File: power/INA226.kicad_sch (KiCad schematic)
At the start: 5 parts, among them U4 INA226

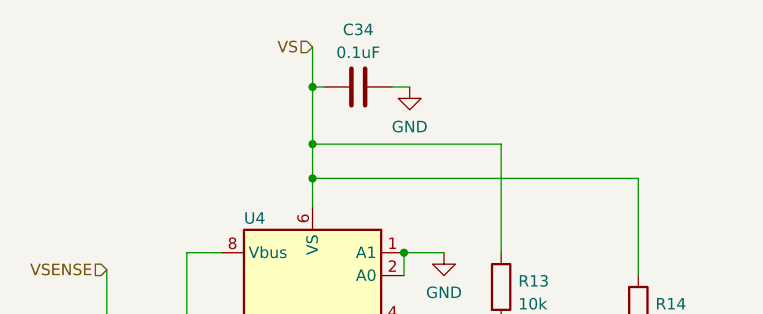
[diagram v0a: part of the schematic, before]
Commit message: Feat: Completed footprint assignment, began part placement
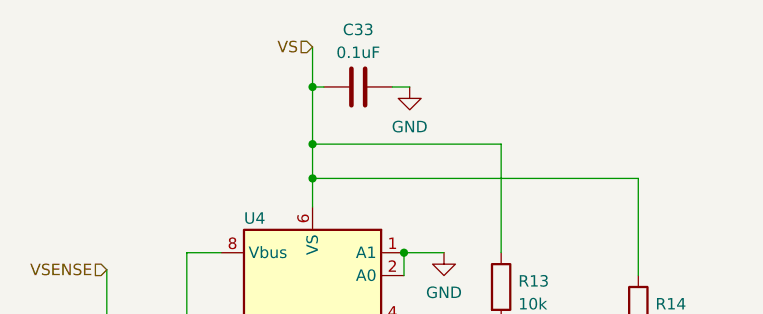
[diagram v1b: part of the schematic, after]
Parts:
- C33: renamed from C34; footprint (none) -> Capacitor_SMD:C_0603_1608Metric
- R13, R14: footprint (none) -> Resistor_SMD:R_0603_1608Metric
- R18: footprint (none) -> Resistor_SMD:R_2512_6332Metric
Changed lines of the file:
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@@
   (symbol (lib_id "Device:C") (at 153.67 64.77 90) (unit 1)
     (in_bom yes) (on_board yes) (dnp no) (fields_autoplaced)
-    (property "Reference" "C34" (at 153.67 58.42 90)
+    (property "Reference" "C33" (at 153.67 58.42 90)
       (effects (font (size 1.27 1.27)))
     )
@@
       (effects (font (size 1.27 1.27)))
     )
-    (property "Footprint" "" (at 157.48 63.8048 0)
+    (property "Footprint" "Capacitor_SMD:C_0603_1608Metric" (at 157.48 63.8048 0)
       (effects (font (size 1.27 1.27)) hide)
     )
@@
       (project "power"
         (path "/6d3c5c52-febb-4c99-82d7-f9b22bb5762b/10807fc9-e13d-42f8-8510-6de977afc8e3"
-          (reference "C34") (unit 1)
+          (reference "C33") (unit 1)
         )
       )
@@
       (effects (font (size 1.27 1.27)) (justify left))
     )
-    (property "Footprint" "" (at 167.767 86.995 90)
+    (property "Footprint" "Resistor_SMD:R_0603_1608Metric" (at 167.767 86.995 90)
       (effects (font (size 1.27 1.27)) hide)
     )
@@
       (effects (font (size 1.27 1.27)) (justify left))
     )
-    (property "Footprint" "" (at 123.952 97.155 90)
+    (property "Footprint" "Resistor_SMD:R_2512_6332Metric" (at 123.952 97.155 90)
       (effects (font (size 1.27 1.27)) hide)
     )
@@
       (effects (font (size 1.27 1.27)) (justify left))
     )
-    (property "Footprint" "" (at 183.007 89.535 90)
+    (property "Footprint" "Resistor_SMD:R_0603_1608Metric" (at 183.007 89.535 90)
       (effects (font (size 1.27 1.27)) hide)
     )

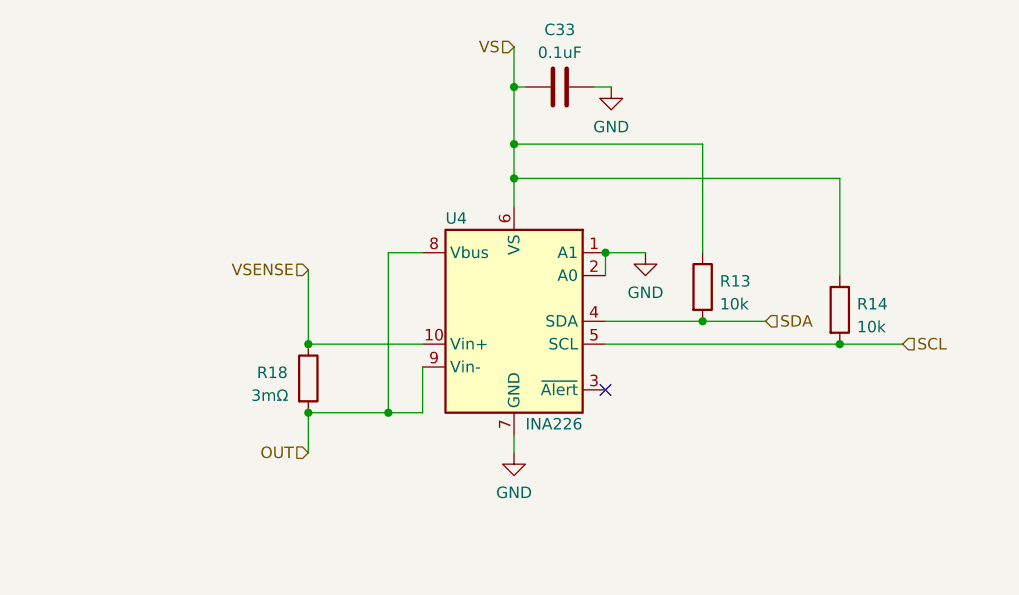
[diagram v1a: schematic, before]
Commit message: Fix: Removed pull up resistors
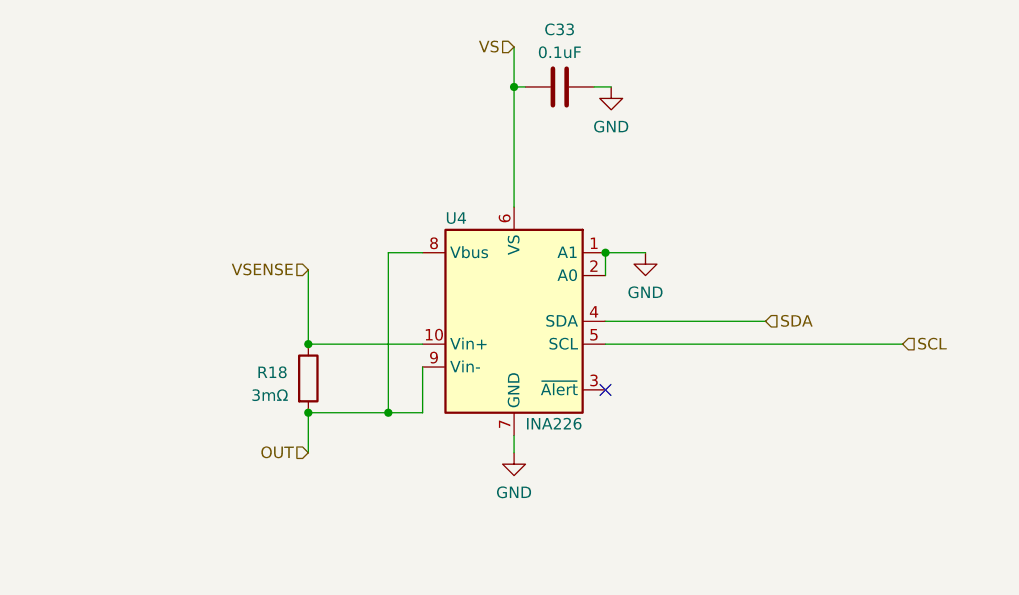
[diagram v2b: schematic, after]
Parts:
- removed R13, R14: 10k, Resistor_SMD:R_0603_1608Metric, symbol Device:R
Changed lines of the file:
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@@
   (junction (at 125.73 93.345) (diameter 0) (color 0 0 0 0)
-  )
-  (junction (at 169.545 90.805) (diameter 0) (color 0 0 0 0)
-  )
-  (junction (at 148.59 71.12) (diameter 0) (color 0 0 0 0)
   )
   (junction (at 134.62 100.965) (diameter 0) (color 0 0 0 0)
@@
   (junction (at 125.73 100.965) (diameter 0) (color 0 0 0 0)
   )
-  (junction (at 148.59 74.93) (diameter 0) (color 0 0 0 0)
-  )
-  (junction (at 184.785 93.345) (diameter 0) (color 0 0 0 0)
-  )
   (no_connect (at 158.75 98.425))
-  (wire (pts (xy 148.59 71.12) (xy 148.59 74.93))
-    (stroke (width 0) (type default))
-  )
-  (wire (pts (xy 148.59 74.93) (xy 148.59 78.105))
-    (stroke (width 0) (type default))
-  )
-  (wire (pts (xy 158.75 90.805) (xy 169.545 90.805))
+  (wire (pts (xy 148.59 64.77) (xy 148.59 78.105))
     (stroke (width 0) (type default))
   )
@@
     (stroke (width 0) (type default))
   )
-  (wire (pts (xy 158.75 93.345) (xy 184.785 93.345))
+  (wire (pts (xy 158.75 93.345) (xy 191.77 93.345))
     (stroke (width 0) (type default))
   )
-  (wire (pts (xy 169.545 90.805) (xy 176.53 90.805))
+  (wire (pts (xy 158.75 90.805) (xy 176.53 90.805))
     (stroke (width 0) (type default))
   )
@@
     (stroke (width 0) (type default))
   )
-  (wire (pts (xy 169.545 71.12) (xy 148.59 71.12))
-    (stroke (width 0) (type default))
-  )
   (wire (pts (xy 125.73 93.345) (xy 138.43 93.345))
-    (stroke (width 0) (type default))
-  )
-  (wire (pts (xy 169.545 83.185) (xy 169.545 71.12))
     (stroke (width 0) (type default))
   )
@@
   )
   (wire (pts (xy 125.73 85.09) (xy 125.73 93.345))
-    (stroke (width 0) (type default))
-  )
-  (wire (pts (xy 184.785 93.345) (xy 191.77 93.345))
     (stroke (width 0) (type default))
   )
@@
     (stroke (width 0) (type default))
   )
-  (wire (pts (xy 184.785 85.725) (xy 184.785 74.93))
-    (stroke (width 0) (type default))
-  )
-  (wire (pts (xy 184.785 74.93) (xy 148.59 74.93))
-    (stroke (width 0) (type default))
-  )
   (wire (pts (xy 158.75 83.185) (xy 163.195 83.185))
     (stroke (width 0) (type default))
@@
   )
   (wire (pts (xy 148.59 64.77) (xy 149.86 64.77))
-    (stroke (width 0) (type default))
-  )
-  (wire (pts (xy 148.59 64.77) (xy 148.59 71.12))
     (stroke (width 0) (type default))
   )
@@
         (path "/6d3c5c52-febb-4c99-82d7-f9b22bb5762b/10807fc9-e13d-42f8-8510-6de977afc8e3"
           (reference "C33") (unit 1)
-        )
-      )
-    )
-  )
-  (symbol (lib_id "Device:R") (at 169.545 86.995 0) (unit 1)
-    (in_bom yes) (on_board yes) (dnp no) (fields_autoplaced)
-    (property "Reference" "R13" (at 171.45 86.36 0)
-      (effects (font (size 1.27 1.27)) (justify left))
-    )
-    (property "Value" "10k" (at 171.45 88.9 0)
-      (effects (font (size 1.27 1.27)) (justify left))
-    )
-    (property "Footprint" "Resistor_SMD:R_0603_1608Metric" (at 167.767 86.995 90)
-      (effects (font (size 1.27 1.27)) hide)
-    )
-    (property "Datasheet" "~" (at 169.545 86.995 0)
-      (effects (font (size 1.27 1.27)) hide)
-    )
-    (pin "1")
-    (pin "2")
-    (instances
-      (project "power"
-        (path "/6d3c5c52-febb-4c99-82d7-f9b22bb5762b/10807fc9-e13d-42f8-8510-6de977afc8e3"
-          (reference "R13") (unit 1)
         )
       )
@@
         )
       )
-    )
-  )
-  (symbol (lib_id "Device:R") (at 184.785 89.535 0) (unit 1)
-    (in_bom yes) (on_board yes) (dnp no) (fields_autoplaced)
-    (property "Reference" "R14" (at 186.69 88.9 0)
-      (effects (font (size 1.27 1.27)) (justify left))
-    )
-    (property "Value" "10k" (at 186.69 91.44 0)
-      (effects (font (size 1.27 1.27)) (justify left))
-    )
-    (property "Footprint" "Resistor_SMD:R_0603_1608Metric" (at 183.007 89.535 90)
-      (effects (font (size 1.27 1.27)) hide)
-    )
-    (property "Datasheet" "~" (at 184.785 89.535 0)
-      (effects (font (size 1.27 1.27)) hide)
-    )
-    (pin "1")
-    (pin "2")
-    (instances
-      (project "power"
-        (path "/6d3c5c52-febb-4c99-82d7-f9b22bb5762b/10807fc9-e13d-42f8-8510-6de977afc8e3"
-          (reference "R14") (unit 1)
-        )
-      )

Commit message: Feat: Switched INA226 i2c address -> 0b1000001
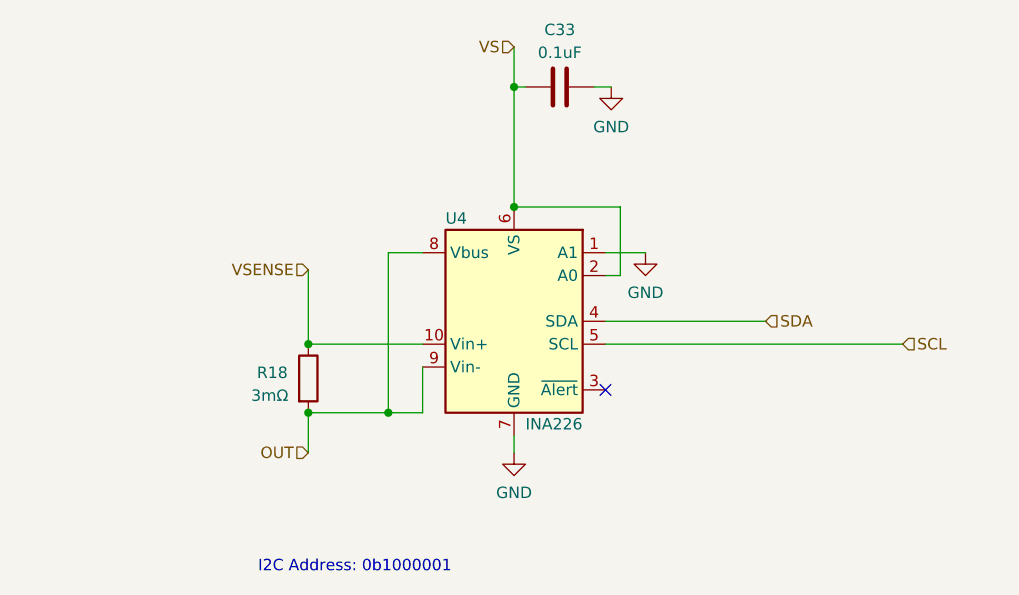
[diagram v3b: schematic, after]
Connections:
- net GND: no longer U4.2 (A0)
- net VS: now also U4.2 (A0)
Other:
- note added: "I2C Address: 0b1000001"
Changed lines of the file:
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@@
 (kicad_sch (version 20230409) (generator eeschema)
   (paper "A4")
+  (junction (at 148.59 78.105) (diameter 0) (color 0 0 0 0)
+  )
   (junction (at 148.59 64.77) (diameter 0) (color 0 0 0 0)
-  )
-  (junction (at 158.75 83.185) (diameter 0) (color 0 0 0 0)
   )
   (junction (at 125.73 93.345) (diameter 0) (color 0 0 0 0)
@@
     (stroke (width 0) (type default))
   )
+  (wire (pts (xy 160.401 85.725) (xy 160.401 78.105))
+    (stroke (width 0) (type default))
+  )
   (wire (pts (xy 134.62 100.965) (xy 138.43 100.965))
     (stroke (width 0) (type default))
   )
   (wire (pts (xy 125.73 93.345) (xy 138.43 93.345))
+    (stroke (width 0) (type default))
+  )
+  (wire (pts (xy 160.401 78.105) (xy 148.59 78.105))
+    (stroke (width 0) (type default))
+  )
+  (wire (pts (xy 158.75 85.725) (xy 160.401 85.725))
     (stroke (width 0) (type default))
   )
@@
     (stroke (width 0) (type default))
   )
-  (wire (pts (xy 158.75 83.185) (xy 158.75 85.725))
-    (stroke (width 0) (type default))
-  )
   (wire (pts (xy 148.59 64.77) (xy 149.86 64.77))
     (stroke (width 0) (type default))
   )
+  (text "I2C Address: 0b1000001" (exclude_from_sim no)
+ (at 120.142 118.872 0)
+    (effects (font (size 1.27 1.27)) (justify left bottom))
+  )
   (hierarchical_label "VSENSE" (shape input) (at 125.73 85.09 180) (fields_autoplaced)

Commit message: Feat: Added jumper for INA226
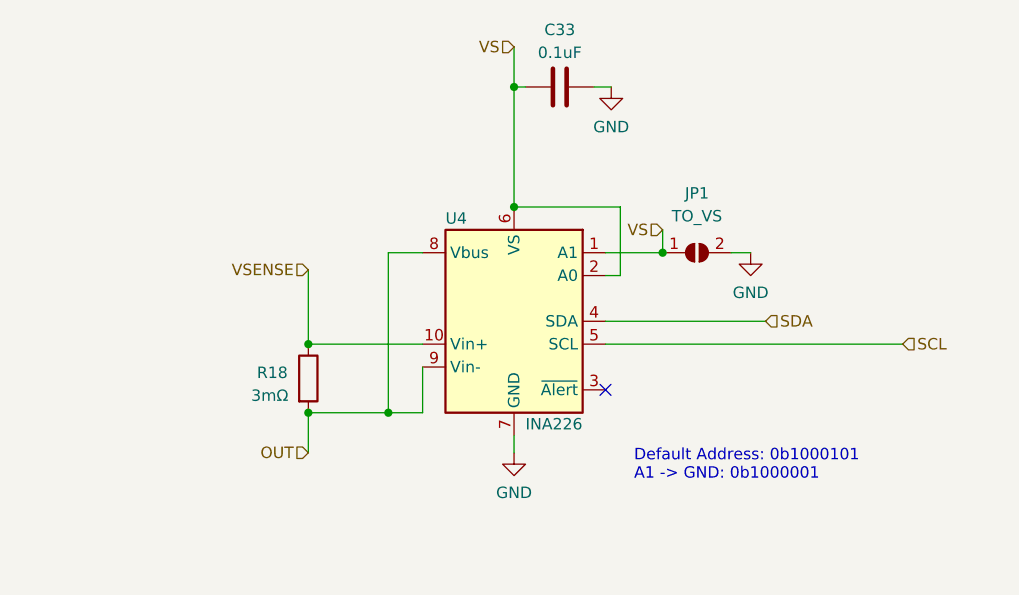
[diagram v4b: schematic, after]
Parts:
- added JP1: TO_VS, Jumper:SolderJumper-2_P1.3mm_Open_RoundedPad1.0x1.5mm, symbol Jumper:SolderJumper_2_Open
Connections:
- net GND: now also JP1.2 (B); no longer U4.1 (A1)
- net VS: now also U4.1 (A1), JP1.1 (A)
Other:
- note added: "Default Address: 0b1000101 A1 -> GND: 0b1000001"
- note removed: "I2C Address: 0b1000001"
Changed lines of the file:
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@@
   (junction (at 125.73 100.965) (diameter 0) (color 0 0 0 0)
+  )
+  (junction (at 165.1 83.185) (diameter 0) (color 0 0 0 0)
   )
   (no_connect (at 158.75 98.425))
@@
     (stroke (width 0) (type default))
   )
-  (wire (pts (xy 158.75 83.185) (xy 163.195 83.185))
+  (wire (pts (xy 165.1 80.645) (xy 165.1 83.185))
+    (stroke (width 0) (type default))
+  )
+  (wire (pts (xy 172.72 83.185) (xy 174.879 83.185))
+    (stroke (width 0) (type default))
+  )
+  (wire (pts (xy 158.75 83.185) (xy 165.1 83.185))
     (stroke (width 0) (type default))
   )
@@
     (stroke (width 0) (type default))
   )
-  (text "I2C Address: 0b1000001" (exclude_from_sim no)
- (at 120.142 118.872 0)
+  (text "Default Address: 0b1000101\nA1 -> GND: 0b1000001" (exclude_from_sim no)
+ (at 161.925 108.585 0)
     (effects (font (size 1.27 1.27)) (justify left bottom))
   )
@@
   )
   (hierarchical_label "OUT" (shape input) (at 125.73 105.41 180) (fields_autoplaced)
+    (effects (font (size 1.27 1.27)) (justify right))
+  )
+  (hierarchical_label "VS" (shape input) (at 165.1 80.645 180) (fields_autoplaced)
     (effects (font (size 1.27 1.27)) (justify right))
   )
@@
     )
   )
+  (symbol (lib_id "Jumper:SolderJumper_2_Open") (at 168.91 83.185 0) (unit 1)
+    (in_bom yes) (on_board yes) (dnp no) (fields_autoplaced)
+    (property "Reference" "JP1" (at 168.91 76.581 0)
+      (effects (font (size 1.27 1.27)))
+    )
+    (property "Value" "TO_VS" (at 168.91 79.121 0)
+      (effects (font (size 1.27 1.27)))
+    )
+    (property "Footprint" "Jumper:SolderJumper-2_P1.3mm_Open_RoundedPad1.0x1.5mm" (at 168.91 83.185 0)
+      (effects (font (size 1.27 1.27)) hide)
+    )
+    (property "Datasheet" "~" (at 168.91 83.185 0)
+      (effects (font (size 1.27 1.27)) hide)
+    )
+    (pin "1")
+    (pin "2")
+    (instances
+      (project "power"
+        (path "/6d3c5c52-febb-4c99-82d7-f9b22bb5762b/10807fc9-e13d-42f8-8510-6de977afc8e3"
+          (reference "JP1") (unit 1)
+        )
+      )
+    )
+  )
   (symbol (lib_id "power:GND") (at 159.385 64.77 0) (unit 1)
     (in_bom yes) (on_board yes) (dnp no)
@@
     )
   )
-  (symbol (lib_id "power:GND") (at 163.195 83.185 0) (unit 1)
-    (in_bom yes) (on_board yes) (dnp no)
-    (property "Reference" "#PWR029" (at 163.195 89.535 0)
-      (effects (font (size 1.27 1.27)) hide)
-    )
-    (property "Value" "GND" (at 163.195 87.63 0)
-      (effects (font (size 1.27 1.27)))
-    )
-    (property "Footprint" "" (at 163.195 83.185 0)
-      (effects (font (size 1.27 1.27)) hide)
-    )
-    (property "Datasheet" "" (at 163.195 83.185 0)
-      (effects (font (size 1.27 1.27)) hide)
-    )
+  (symbol (lib_id "power:GND") (at 174.879 83.185 0) (unit 1)
+    (in_bom yes) (on_board yes) (dnp no)
+    (property "Reference" "#PWR029" (at 174.879 89.535 0)
+      (effects (font (size 1.27 1.27)) hide)
+    )
+    (property "Value" "GND" (at 174.879 87.63 0)
+      (effects (font (size 1.27 1.27)))
+    )
+    (property "Footprint" "" (at 174.879 83.185 0)
+      (effects (font (size 1.27 1.27)) hide)
+    )
+    (property "Datasheet" "" (at 174.879 83.185 0)
+      (effects (font (size 1.27 1.27)) hide)
+    )
